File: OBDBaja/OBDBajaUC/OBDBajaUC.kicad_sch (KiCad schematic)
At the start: 9 parts, among them J1 Conn_01x01, J3 Conn_01x10, J4 Conn_01x01, J5 Conn_01x02, J5 Conn_01x14, J6 Conn_01x01, U1 Teensy4.0

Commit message: Updated OBD Baja file organization
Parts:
- J1, J4, J6: footprint Connector_PinHeader_2.54mm:PinHeader_1x01_P2.54mm_Vertical -> Connector_PinHeader_2.54mm:PinHeader_1x01_P2.54mm_Horizontal
- J5: footprint Connector_PinHeader_2.54mm:PinHeader_1x14_P2.54mm_Vertical -> Connector_PinSocket_2.54mm:PinSocket_1x14_P2.54mm_Vertical
- J5: footprint Connector_PinHeader_2.54mm:PinHeader_1x02_P2.54mm_Vertical -> Connector_PinHeader_2.54mm:PinHeader_1x02_P2.54mm_Horizontal
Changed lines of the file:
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@@
       (effects (font (size 1.27 1.27)) (justify left))
     )
-    (property "Footprint" "Connector_PinHeader_2.54mm:PinHeader_1x01_P2.54mm_Vertical" (at 78.105 131.445 0)
+    (property "Footprint" "Connector_PinHeader_2.54mm:PinHeader_1x01_P2.54mm_Horizontal" (at 78.105 131.445 0)
       (effects (font (size 1.27 1.27)) hide)
     )
@@
       (effects (font (size 1.27 1.27)) (justify left))
     )
-    (property "Footprint" "Connector_PinHeader_2.54mm:PinHeader_1x01_P2.54mm_Vertical" (at 78.105 125.095 0)
+    (property "Footprint" "Connector_PinHeader_2.54mm:PinHeader_1x01_P2.54mm_Horizontal" (at 78.105 125.095 0)
       (effects (font (size 1.27 1.27)) hide)
     )
@@
       (effects (font (size 1.27 1.27)))
     )
-    (property "Footprint" "Connector_PinHeader_2.54mm:PinHeader_1x14_P2.54mm_Vertical" (at 149.86 158.75 0)
+    (property "Footprint" "Connector_PinSocket_2.54mm:PinSocket_1x14_P2.54mm_Vertical" (at 149.86 158.75 0)
       (effects (font (size 1.27 1.27)) hide)
     )
@@
       (effects (font (size 1.27 1.27)) (justify left))
     )
-    (property "Footprint" "Connector_PinHeader_2.54mm:PinHeader_1x01_P2.54mm_Vertical" (at 78.105 128.27 0)
+    (property "Footprint" "Connector_PinHeader_2.54mm:PinHeader_1x01_P2.54mm_Horizontal" (at 78.105 128.27 0)
       (effects (font (size 1.27 1.27)) hide)
     )
@@
       (effects (font (size 1.27 1.27)) (justify left))
     )
-    (property "Footprint" "Connector_PinHeader_2.54mm:PinHeader_1x02_P2.54mm_Vertical" (at 114.3 69.85 0)
-      (effects (font (size 1.27 1.27)) hide)
-    )
+    (property "Footprint" "Connector_PinHeader_2.54mm:PinHeader_1x02_P2.54mm_Horizontal" (at 114.3 69.85 0)
+      (effects (font (size 1.27 1.27)) hide)
+    )

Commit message: Finished PCB and test enclosure
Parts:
- added J7: Conn_01x06, Connector_PinHeader_2.54mm:PinHeader_1x06_P2.54mm_Horizontal, symbol Connector_Generic:Conn_01x06
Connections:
- net GND: now also J7.6 (Pin_6)
- net UP: now reaches U1.26 (19_A5_SCL0)
- net UP: now also J7.1 (Pin_1)
- net DN: now reaches U1.27 (20_A6_TX5_LRCLK1)
- net DN: now also J7.2 (Pin_2)
- net L: now reaches U1.28 (21_A7_RX5_BCLK1)
- net L: now also J7.3 (Pin_3)
- net R: now reaches U1.29 (22_A8_CTX1)
- net R: now also J7.4 (Pin_4)
- net SEL: now reaches U1.30 (23_A9_CRX1_MCLK1)
- net SEL: now also J7.5 (Pin_5)
- no-connect marks 29 -> 24

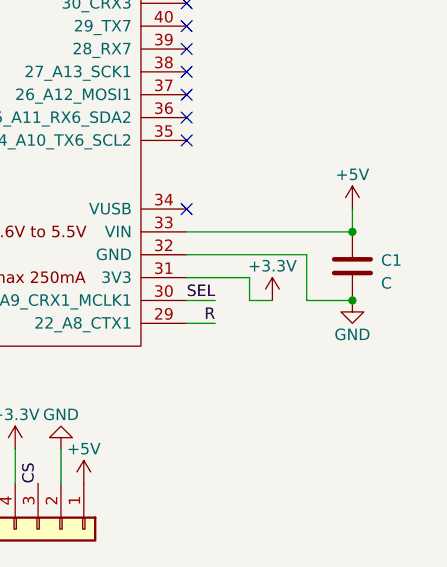
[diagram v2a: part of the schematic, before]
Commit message: Added images
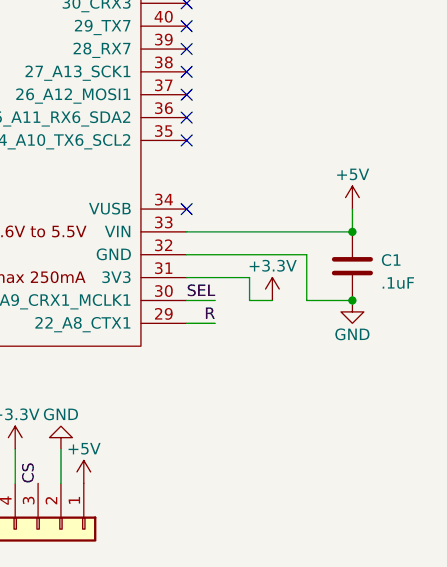
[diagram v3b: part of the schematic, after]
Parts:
- C1: value C -> .1uF
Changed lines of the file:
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@@
       (effects (font (size 1.27 1.27)) (justify right))
     )
-    (property "Value" "C" (at 198.12 131.445 0)
+    (property "Value" ".1uF" (at 198.12 131.445 0)
       (effects (font (size 1.27 1.27)) (justify right))
     )
